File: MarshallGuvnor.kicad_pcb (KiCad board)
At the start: 4 copper layers, 85 x 56 mm, 51 parts, among them J1 POWER, J2 INPUT, J3 OUTPUT, Q1 IRFD9120 PMOS, U1 TL084

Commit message: Minor bugfixes
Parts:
- moved J2 5.01 mm to (106.3, 135.0), turned to -90 degrees
- moved J1 4.79 mm to (106.3, 115.5), turned to -90 degrees
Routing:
- net Net-(J1-Pin_1): track 11.7 -> 16.2 mm
- net Net-(J2-Pin_1): track 43.0 -> 41.0 mm
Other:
- board text added: "+ INPUT -"
- board text added: "+ POWER -"
- board text added: "JLCJLCJLC"
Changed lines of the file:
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@@
     (pad "2" thru_hole circle locked (at 2.54 0) (size 1.8 1.8) (drill 0.9) (layers "*.Cu" "*.Mask")
       (net 12 "+9V") (pinfunction "A") (pintype "passive"))
-    (model "${KICAD6_3DMODEL_DIR}/LED_THT.3dshapes/LED_D5.0mm_FlatTop.wrl"
+    (model "${KICAD6_3DMODEL_DIR}/LED_THT.3dshapes/LED_D5.0mm_FlatTop.wrl" hide
+      (offset (xyz 0 0 0))
+      (scale (xyz 1 1 1))
+      (rotate (xyz 0 0 0))
+    )
+    (model "${KICAD6_3DMODEL_DIR}/LED_THT.3dshapes/LED_D5.0mm_Clear.wrl"
       (offset (xyz 0 0 0))
       (scale (xyz 1 1 1))
@@
     )
   )
-  (footprint "Connector_JST:JST_NV_B02P-NV_1x02_P5.00mm_Vertical" locked (layer "F.Cu")
-    (at 106 120.2775 90)
+  (footprint "Connector_JST:JST_NV_B02P-NV_1x02_P5.00mm_Vertical" (layer "F.Cu")
+    (at 106.35 115.5 -90)
     (descr "JST NV series connector, B02P-NV (http://www.jst-mfg.com/product/pdf/eng/eNV.pdf), generated with kicad-footprint-generator")
     (tags "connector JST NV side entry")
@@
     (fp_line (start 7.5 4.8) (end 7.5 -3.7)
       (stroke (width 0.1) (type solid)) (layer "F.Fab"))
-    (pad "1" thru_hole roundrect locked (at 0 0 90) (size 2.7 2.7) (drill 1.7) (layers "*.Cu" "*.Mask") (roundrect_rratio 0.09259296296)
+    (pad "1" thru_hole roundrect (at 0 0 270) (size 2.7 2.7) (drill 1.7) (layers "*.Cu" "*.Mask") (roundrect_rratio 0.09259296296)
       (net 16 "Net-(J1-Pin_1)") (pinfunction "Pin_1") (pintype "passive"))
-    (pad "2" thru_hole circle locked (at 5 0 90) (size 2.7 2.7) (drill 1.7) (layers "*.Cu" "*.Mask")
+    (pad "2" thru_hole circle (at 5 0 270) (size 2.7 2.7) (drill 1.7) (layers "*.Cu" "*.Mask")
       (net 2 "GND") (pinfunction "Pin_2") (pintype "passive"))
-    (model "${KICAD6_3DMODEL_DIR}/Connector_JST.3dshapes/JST_NV_B02P-NV_1x02_P5.00mm_Vertical.wrl"
+    (model ":KICAD7_3DMODEL_DIR:TerminalBlock_Phoenix.3dshapes/TerminalBlock_Phoenix_MKDS-1,5-2_1x02_P5.00mm_Horizontal.step"
       (offset (xyz 0 0 0))
       (scale (xyz 1 1 1))
@@
     )
   )
-  (footprint "Connector_JST:JST_NV_B02P-NV_1x02_P5.00mm_Vertical" locked (layer "F.Cu")
-    (at 106 140 90)
+  (footprint "Connector_JST:JST_NV_B02P-NV_1x02_P5.00mm_Vertical" (layer "F.Cu")
+    (at 106.35 135 -90)
     (descr "JST NV series connector, B02P-NV (http://www.jst-mfg.com/product/pdf/eng/eNV.pdf), generated with kicad-footprint-generator")
     (tags "connector JST NV side entry")
@@
     (fp_line (start 7.5 4.8) (end 7.5 -3.7)
       (stroke (width 0.1) (type solid)) (layer "F.Fab"))
-    (pad "1" thru_hole roundrect locked (at 0 0 90) (size 2.7 2.7) (drill 1.7) (layers "*.Cu" "*.Mask") (roundrect_rratio 0.09259296296)
+    (pad "1" thru_hole roundrect (at 0 0 270) (size 2.7 2.7) (drill 1.7) (layers "*.Cu" "*.Mask") (roundrect_rratio 0.09259296296)
       (net 3 "Net-(J2-Pin_1)") (pinfunction "Pin_1") (pintype "passive"))
-    (pad "2" thru_hole circle locked (at 5 0 90) (size 2.7 2.7) (drill 1.7) (layers "*.Cu" "*.Mask")
+    (pad "2" thru_hole circle (at 5 0 270) (size 2.7 2.7) (drill 1.7) (layers "*.Cu" "*.Mask")
       (net 2 "GND") (pinfunction "Pin_2") (pintype "passive"))
-    (model "${KICAD6_3DMODEL_DIR}/Connector_JST.3dshapes/JST_NV_B02P-NV_1x02_P5.00mm_Vertical.wrl"
+    (model ":KICAD7_3DMODEL_DIR:TerminalBlock_Phoenix.3dshapes/TerminalBlock_Phoenix_MKDS-1,5-2_1x02_P5.00mm_Horizontal.step"
       (offset (xyz 0 0 0))
       (scale (xyz 1 1 1))
@@
     (pad "2" thru_hole circle locked (at 5 0 90) (size 2.7 2.7) (drill 1.7) (layers "*.Cu" "*.Mask")
       (net 10 "Net-(J3-Pin_2)") (pinfunction "Pin_2") (pintype "passive"))
-    (model "${KICAD6_3DMODEL_DIR}/Connector_JST.3dshapes/JST_NV_B02P-NV_1x02_P5.00mm_Vertical.wrl"
+    (model ":KICAD7_3DMODEL_DIR:TerminalBlock_Phoenix.3dshapes/TerminalBlock_Phoenix_MKDS-1,5-2_1x02_P5.00mm_Horizontal.step"
       (offset (xyz 0 0 0))
       (scale (xyz 1 1 1))
@@
   (gr_line locked (start 180 100) (end 105 100)
     (stroke (width 0.1) (type default)) (layer "Edge.Cuts"))
-  (gr_text locked "- POWER +" (at 100.5 117.5 270) (layer "F.SilkS")
+  (gr_text "+ POWER -" (at 100 118 270) (layer "F.SilkS")
     (effects (font (size 1 1) (thickness 0.2) bold) (justify bottom))
   )
@@
     (effects (font (size 1.8 1.8) (thickness 0.375) bold) (justify bottom))
   )
+  (gr_text "JLCJLCJLC" (at 139 148) (layer "F.SilkS")
+    (effects (font (size 1 1) (thickness 0.15)) (justify left bottom))
+  )
   (gr_text locked "- OUTPUT +" (at 184.411441 140.022222 90) (layer "F.SilkS")
     (effects (font (size 1 1) (thickness 0.2) bold) (justify bottom))
@@
     (effects (font (size 1 1) (thickness 0.2) bold) (justify bottom))
   )
-  (gr_text locked "- INPUT +" (at 100.5 137.5 270) (layer "F.SilkS")
+  (gr_text "+ INPUT -" (at 100 137.5 270) (layer "F.SilkS")
     (effects (font (size 1 1) (thickness 0.2) bold) (justify bottom))
   )
@@
   (via (at 147 122.2) (size 0.8) (drill 0.4) (layers "F.Cu" "B.Cu") (net 2))
   (segment (start 137.2 132) (end 138.2 131) (width 0.6) (layer "F.Cu") (net 3))
+  (segment (start 106 135) (end 112 135) (width 0.6) (layer "F.Cu") (net 3))
   (segment (start 136.7625 132) (end 137.2 132) (width 0.6) (layer "F.Cu") (net 3))
+  (segment (start 115 132) (end 136.7625 132) (width 0.6) (layer "F.Cu") (net 3))
   (segment (start 138.2 131) (end 138.2 125.95) (width 0.6) (layer "F.Cu") (net 3))
-  (segment (start 106 140) (end 110.8 140) (width 0.6) (layer "F.Cu") (net 3))
   (segment (start 138.2 125.95) (end 136.75 124.5) (width 0.6) (layer "F.Cu") (net 3))
-  (segment (start 110.8 140) (end 118.8 132) (width 0.6) (layer "F.Cu") (net 3))
-  (segment (start 118.8 132) (end 136.7625 132) (width 0.6) (layer "F.Cu") (net 3))
+  (segment (start 112 135) (end 115 132) (width 0.6) (layer "F.Cu") (net 3))
   (segment (start 147.4 127) (end 152 127) (width 0.6) (layer "F.Cu") (net 4))
   (segment (start 139.7 124.5) (end 139.7 128.2375) (width 0.6) (layer "F.Cu") (net 4))
@@
   (segment (start 159 107) (end 159 105) (width 0.6) (layer "B.Cu") (net 15))
   (segment (start 164 147.4) (end 164 112) (width 0.6) (layer "B.Cu") (net 15))
-  (segment (start 109.5275 120.2775) (end 110.27 121.02) (width 1.6) (layer "F.Cu") (net 16))
-  (segment (start 106 120.2775) (end 109.5275 120.2775) (width 1.6) (layer "F.Cu") (net 16))
-  (segment (start 110.27 121.02) (end 117.3675 121.02) (width 1.6) (layer "F.Cu") (net 16))
+  (segment (start 115.02 121.02) (end 119.9075 121.02) (width 1.6) (layer "F.Cu") (net 16))
+  (segment (start 109.5 115.5) (end 115.02 121.02) (width 1.6) (layer "F.Cu") (net 16))
+  (segment (start 106 115.5) (end 109.5 115.5) (width 1.6) (layer "F.Cu") (net 16))
   (segment (start 148 151) (end 157.725 141.275) (width 0.6) (layer "F.Cu") (net 17))
   (segment (start 157.725 141.275) (end 157.725 139.9375) (width 0.6) (layer "F.Cu") (net 17))
@@
     )
   )
-  (group "" locked (id 5491ec0d-6e8a-48e5-9ab2-86a2bc89d61b)
-    (members
-      01fcda78-3a9d-4eb1-9540-92cb847dc504
-      835048ab-e840-4af1-8db2-2db1e1f01ccd
-    )
-  )
   (group "" locked (id 790a6eea-28de-457e-a57e-0538c2505c9b)
     (members
@@
     )
   )
-  (group "" locked (id bacdd362-f447-40eb-9f60-ebec225fe73e)
-    (members
-      61697e58-160e-478c-a370-8fb30410cc4c
-      a275ad3f-a929-421e-ad19-10b09ad932bf
-    )
-  )

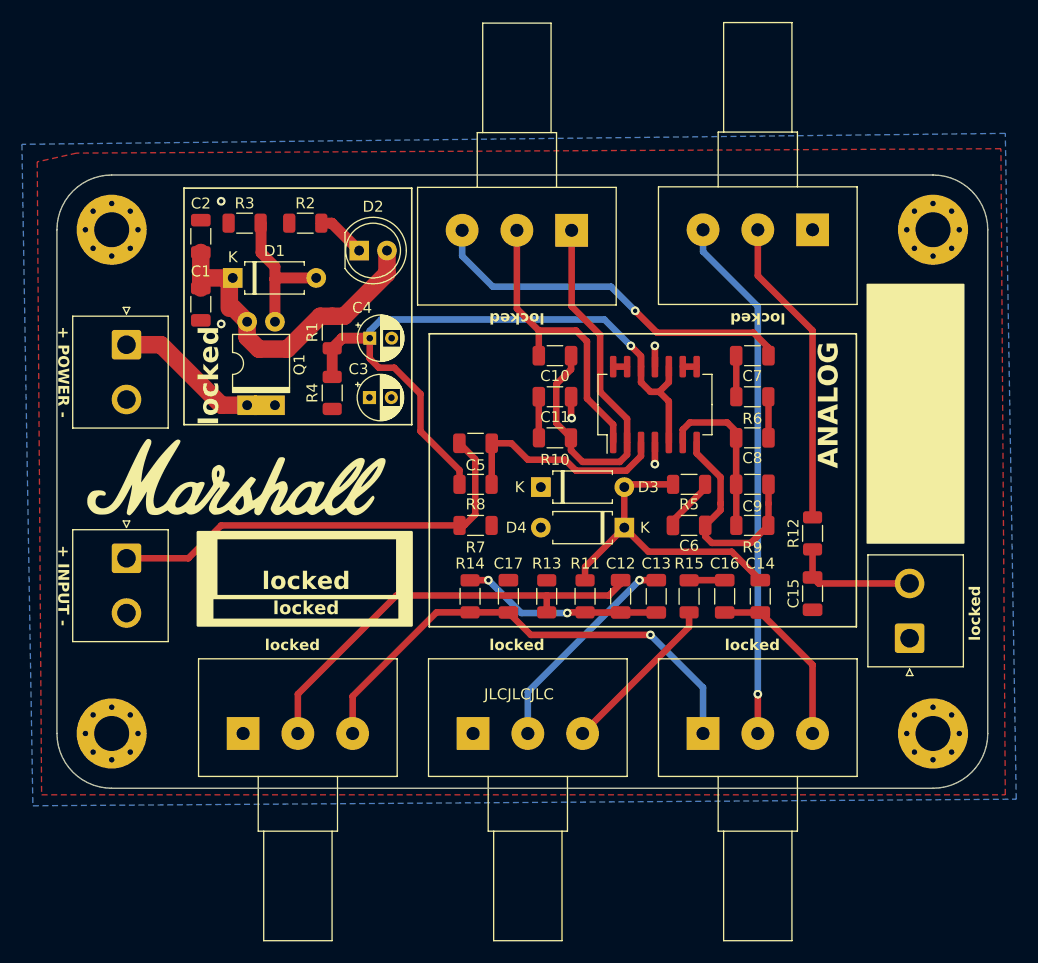
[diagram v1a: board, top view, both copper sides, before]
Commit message: Update shcm, change one cap value, add footswitch
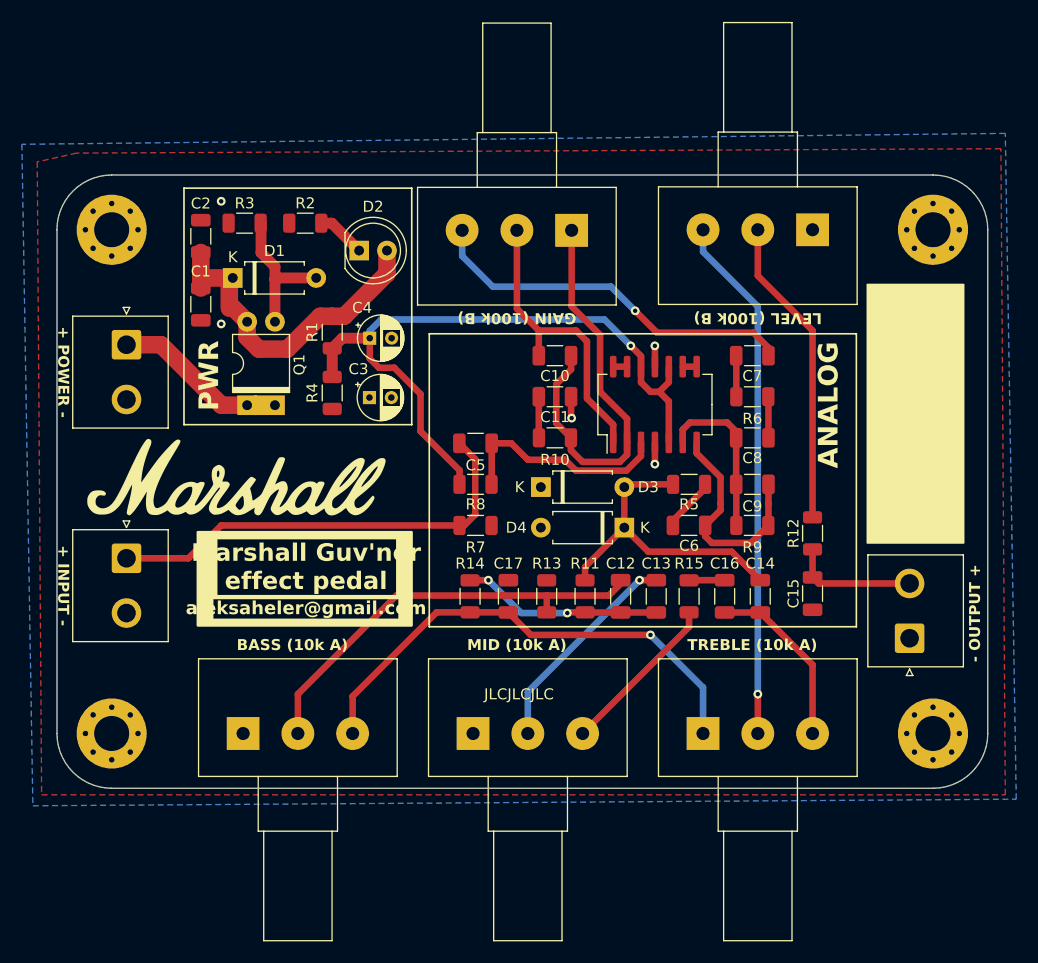
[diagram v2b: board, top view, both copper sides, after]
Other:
- board text added: "- OUTPUT +"
- board text added: "BASS (10k A)"
- board text added: "GAIN (100k B)"
- board text added: "LEVEL (100k B)"
- board text added: "MID (10k A)"
- board text added: "Marshall Guv'nor effect pedal"
- board text added: "PWR"
- board text added: "TREBLE (10k A)"
- board text added: "aleksaheler@gmail.com"
- board text removed: "locked"
